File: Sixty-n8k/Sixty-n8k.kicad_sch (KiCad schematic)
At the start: 71 parts, among them J1 USB4085-GF-A_REVB, J2 SD_CARD_PORT, J3 Conn_02x32_Odd_Even, J4 Conn_01x02, SW1 RESET, SW2 DEBUG, U1 74LS05, U10 74HC164, U11 74LS393, U13 74LS148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

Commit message: Simplified design, relaid out, re-routed
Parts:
- removed C24, C25: 100nf, Capacitor_THT:C_Disc_D5.0mm_W2.5mm_P2.50mm, symbol Device:C_Small
- removed U15: 74LS138, Package_DIP:DIP-16_W7.62mm_Socket, symbol 74xx:74LS138
- removed U18: ATF16V8BQL-15PI, Package_DIP:DIP-20_W7.62mm_Socket, symbol ATF16V8BQL_15:ATF16V8BQL-15PI
- removed U5: 74LS32, Package_DIP:DIP-14_W7.62mm_Socket, symbol 74xx:74LS32
- added U12: 22V10C, Package_DIP:DIP-24_W7.62mm_Socket, symbol n8-bit-special-rescue:22V10C-6502
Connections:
- net ~{IACK} is gone; now on net ~{AS}: U16.5 (E2)
- net +5V: now also U19.9, U12.24 (VCC); no longer U16.6 (E3)
- net A16: now also U12.1 (CLK/IN1)
- net A17: now also U12.2 (IN2)
- net A18: now also U12.3 (IN3)
- net A19: now also U12.4 (IN4/PD)
- net A20: now also U12.5 (IN5)
- net A21: now also U12.6 (IN6)
- net A22: now also U12.7 (IN7)
- net A23: now also U12.8 (IN8)
- net BERR_WATCHDOG: now also RN2.2 (R1); no longer RN2.6 (R5)
- net CLK_{HALF}: now also J3.50 (Pin_50); no longer J3.18 (Pin_18)
- net D0: now also J3.6 (Pin_6); no longer J3.60 (Pin_60)
- net D1: now also J3.8 (Pin_8); no longer J3.58 (Pin_58)
- net D10: now also J3.26 (Pin_26); no longer J3.40 (Pin_40)
- net D11: now also J3.28 (Pin_28); no longer J3.38 (Pin_38)
- net D12: now also J3.30 (Pin_30); no longer J3.36 (Pin_36)
- net D13: now also J3.32 (Pin_32); no longer J3.34 (Pin_34)
- net D14: now also J3.34 (Pin_34); no longer J3.32 (Pin_32)
- net D15: now also J3.36 (Pin_36); no longer J3.30 (Pin_30)
- net D2: now also J3.10 (Pin_10); no longer J3.56 (Pin_56)
- net D3: now also J3.12 (Pin_12); no longer J3.54 (Pin_54)
- net D4: now also J3.14 (Pin_14); no longer J3.52 (Pin_52)
- net D5: now also J3.16 (Pin_16); no longer J3.50 (Pin_50)
- net D6: now also J3.18 (Pin_18); no longer J3.48 (Pin_48)
- net D7: now also J3.20 (Pin_20); no longer J3.46 (Pin_46)
- net D8: now also J3.22 (Pin_22); no longer J3.44 (Pin_44)
- net D9: now also J3.24 (Pin_24); no longer J3.42 (Pin_42)
- net FC0: now also U19.13
- net FC1: now also U19.12
- net FC2: now also U19.10
- net GND: now also U16.4 (E1), U12.12 (GND); no longer U19.10, U19.12, U19.13, U19.9
- net HALT: now also RN2.5 (R4); no longer RN2.3 (R2)
- net R~{W}: now also J3.11 (Pin_11), RN3.5 (R4), U12.15 (IO14); no longer J3.9 (Pin_9), RN3.6 (R5)
- net ~{AS}: now also J3.5 (Pin_5), RN3.2 (R1), U12.9 (IN9); no longer J3.11 (Pin_11), RN3.9 (R8), U16.4 (E1)
- net ~{BERR}: now also J3.44 (Pin_44), RN3.6 (R5); no longer J3.12 (Pin_12), RN2.5 (R4)
- net ~{BGACK}: now also J3.60 (Pin_60), RN3.8 (R7); no longer J3.28 (Pin_28), RN3.3 (R2)
- net ~{BG}: now also J3.40 (Pin_40); no longer J3.8 (Pin_8)
- net ~{BR}: now also J3.42 (Pin_42), RN3.9 (R8); no longer J3.10 (Pin_10), RN3.2 (R1)
- net ~{CS_MFP}: now also U12.23 (IO22)
- net ~{CS_XPN}: now also U12.18 (IO17)
- net ~{HALT}: now also RN2.4 (R3); no longer RN2.2 (R1)
- net ~{IACK_HI}: now also J3.58 (Pin_58); no longer J3.26 (Pin_26)
- net ~{IACK_LOW}: now also J3.56 (Pin_56); no longer J3.24 (Pin_24)
- net ~{IRQ_HI}: now also J3.54 (Pin_54), RN1.8 (R7), RN2.7 (R6); no longer J3.22 (Pin_22), RN1.3 (R2), RN3.5 (R4)
- net ~{IRQ_LOW}: now also J3.52 (Pin_52), RN1.3 (R2), RN2.3 (R2); no longer J3.20 (Pin_20), RN1.8 (R7), RN3.4 (R3)
- net ~{IRQ_MFP}: now also RN1.6 (R5); no longer RN1.5 (R4)
- net ~{LDS}: now also J3.9 (Pin_9), RN3.4 (R3), U12.10 (IN10); no longer J3.5 (Pin_5), RN3.7 (R6)
- net ~{RES}: now also RN2.6 (R5); no longer RN2.4 (R3)
- net ~{ROM_OVERLAY}: now also U12.14 (IO13)
- net ~{UDS}: now also RN3.3 (R2), U12.11 (IN11); no longer RN3.8 (R7)
- net ~{VPA}: now also RN3.7 (R6); no longer RN2.7 (R6)
- net ~{CS_RAM}_{ODD}: now reaches U4.22 (CE#), U4.24 (OE#)
- net ~{CS_RAM}_{ODD}: now also U12.19 (IO18)
- net ~{CS_RAM}_{EVEN}: now reaches U7.22 (CE#), U7.24 (OE#)
- net ~{CS_RAM}_{EVEN}: now also U12.20 (IO19)
- net ~{CS_ROM}_{EVEN}: now reaches U8.22 (~{CE}), U8.24 (~{OE})
- net ~{CS_ROM}_{EVEN}: now also U12.22 (IO21)
- net ~{CS_ROM}_{ODD}: now reaches U3.22 (~{CE}), U3.24 (~{OE})
- net ~{CS_ROM}_{ODD}: now also U12.21 (IO20)
- net IACK: now reaches U19.8
- net IACK: now also U16.6 (E3), U12.13 (IN12)
- net at U13.12 (I2): now also RN1.4 (R3); no longer RN1.7 (R6)
- net at U13.13 (I3): now also RN1.5 (R4); no longer RN1.6 (R5)
- net at U13.2 (I5): now also RN1.7 (R6); no longer RN1.4 (R3)
- net at U1.6, U13.4 (I7): now also RN1.9 (R8); no longer RN1.2 (R1)
- no-connect marks 62 -> 54
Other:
- moved on the sheet: U11C, U19A, U19B, U19C, U1G

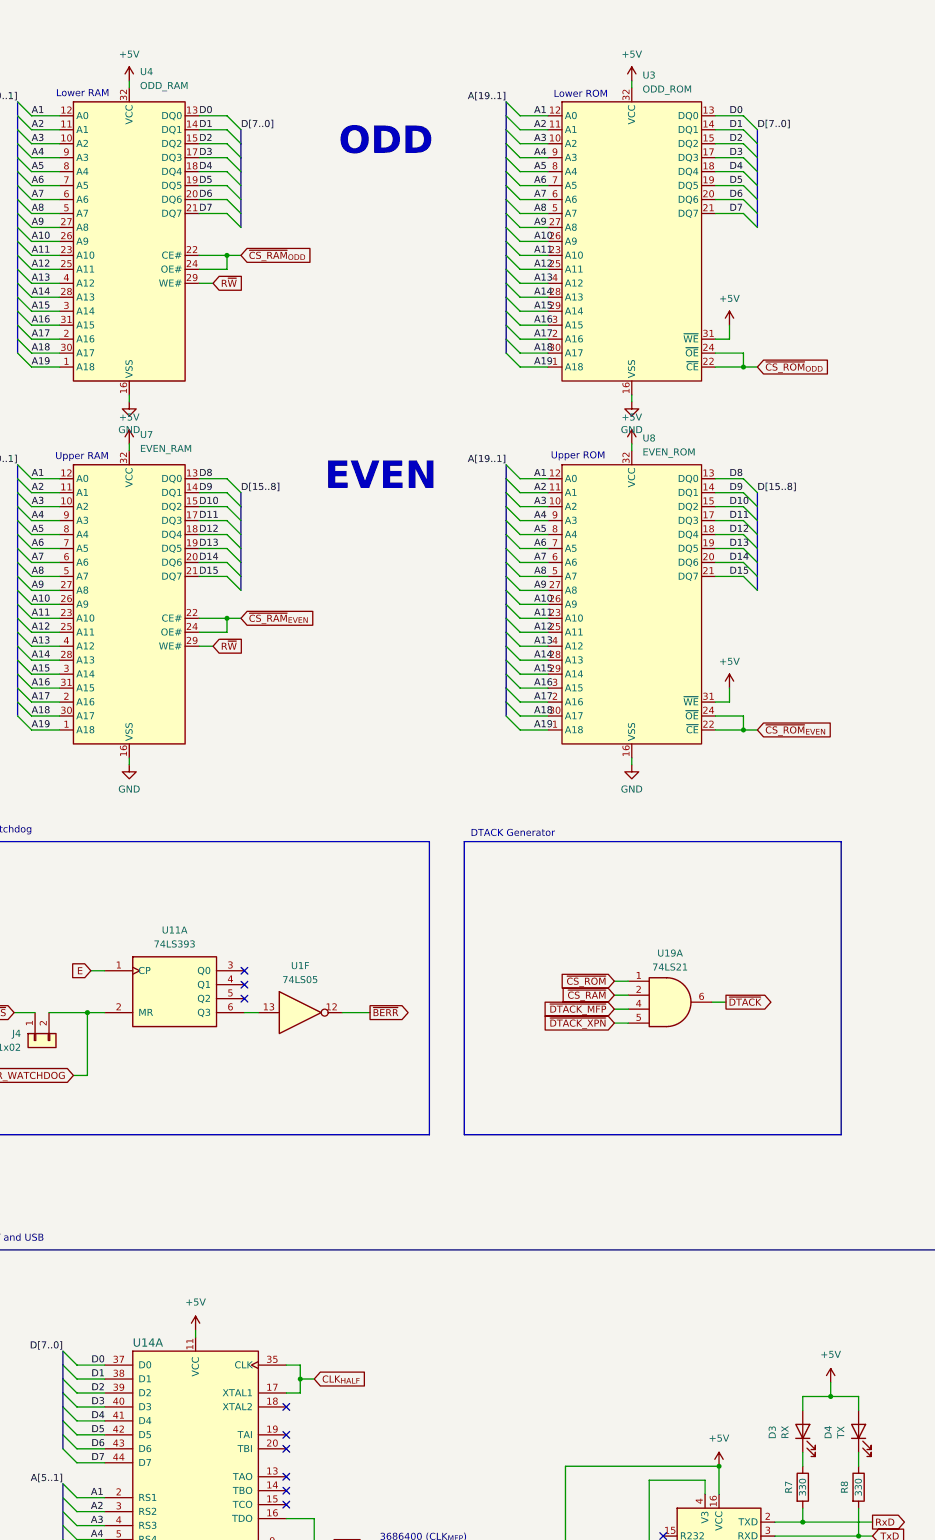
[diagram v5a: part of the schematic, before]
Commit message: More sane layout and further reductions
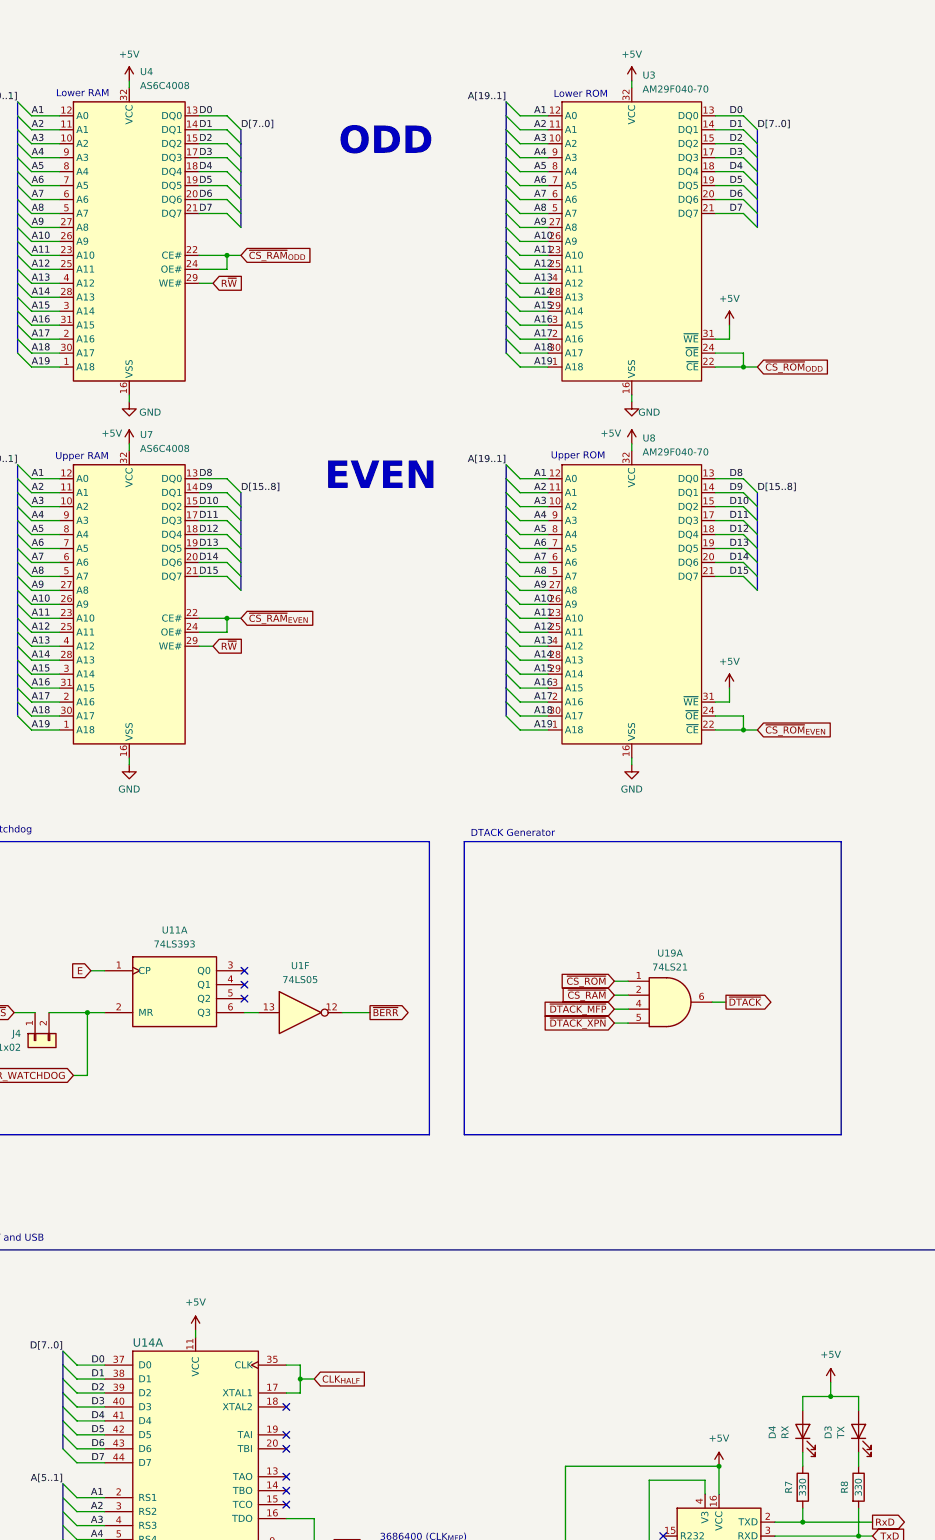
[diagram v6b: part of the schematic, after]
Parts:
- U3: value ODD_ROM -> AM29F040-70
- U4: value ODD_RAM -> AS6C4008
- U7: value EVEN_RAM -> AS6C4008
- U8: value EVEN_ROM -> AM29F040-70
- renumbered D4 to D3, D3 to D4
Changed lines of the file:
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@@
   )
   (symbol (lib_id "power:+5V") (at 431.8 95.25 0) (unit 1)
-    (in_bom yes) (on_board yes) (dnp no) (fields_autoplaced)
+    (in_bom yes) (on_board yes) (dnp no)
     (property "Reference" "#PWR020" (at 431.8 99.06 0)
       (effects (font (size 1.27 1.27)) hide)
     )
-    (property "Value" "+5V" (at 431.8 90.424 0)
+    (property "Value" "+5V" (at 427.99 93.345 0)
       (effects (font (size 1.27 1.27)))
     )
@@
       (effects (font (size 1.27 1.27)) hide)
     )
-    (property "Value" "GND" (at 340.36 92.71 0)
+    (property "Value" "GND" (at 344.17 89.535 0)
       (effects (font (size 1.27 1.27)))
     )
@@
       (effects (font (size 1.27 1.27)) (justify left))
     )
-    (property "Value" "ODD_RAM" (at 342.3159 30.099 0)
+    (property "Value" "AS6C4008" (at 342.3159 30.099 0)
       (effects (font (size 1.27 1.27)) (justify left))
     )
@@
   (symbol (lib_id "Device:LED") (at 473.075 274.955 90) (unit 1)
     (in_bom yes) (on_board yes) (dnp no)
-    (property "Reference" "D4" (at 467.5632 275.1328 0)
+    (property "Reference" "D3" (at 467.5632 275.1328 0)
       (effects (font (size 1.27 1.27)))
     )
@@
       (project "Sixty-n8k"
         (path "/899701f7-f496-45c9-a35e-7f376afd1eaf"
-          (reference "D4") (unit 1)
+          (reference "D3") (unit 1)
         )
       )
@@
   (symbol (lib_id "Device:LED") (at 462.915 274.955 90) (unit 1)
     (in_bom yes) (on_board yes) (dnp no)
-    (property "Reference" "D3" (at 457.4032 275.1328 0)
+    (property "Reference" "D4" (at 457.4032 275.1328 0)
       (effects (font (size 1.27 1.27)))
     )
@@
       (project "Sixty-n8k"
         (path "/899701f7-f496-45c9-a35e-7f376afd1eaf"
-          (reference "D3") (unit 1)
+          (reference "D4") (unit 1)
         )
       )
@@
       (effects (font (size 1.27 1.27)) (justify left))
     )
-    (property "Value" "EVEN_ROM" (at 433.7559 96.774 0)
+    (property "Value" "AM29F040-70" (at 433.7559 96.774 0)
       (effects (font (size 1.27 1.27)) (justify left))
     )
@@
   )
   (symbol (lib_id "power:GND") (at 431.8 87.63 0) (unit 1)
-    (in_bom yes) (on_board yes) (dnp no) (fields_autoplaced)
+    (in_bom yes) (on_board yes) (dnp no)
     (property "Reference" "#PWR016" (at 431.8 93.98 0)
       (effects (font (size 1.27 1.27)) hide)
     )
-    (property "Value" "GND" (at 431.8 92.71 0)
+    (property "Value" "GND" (at 434.975 89.535 0)
       (effects (font (size 1.27 1.27)))
     )
@@
       (effects (font (size 1.27 1.27)) (justify left))
     )
-    (property "Value" "ODD_ROM" (at 433.7559 30.734 0)
+    (property "Value" "AM29F040-70" (at 433.7559 30.734 0)
       (effects (font (size 1.27 1.27)) (justify left))
     )
@@
   )
   (symbol (lib_id "power:+5V") (at 340.36 95.25 0) (unit 1)
-    (in_bom yes) (on_board yes) (dnp no) (fields_autoplaced)
+    (in_bom yes) (on_board yes) (dnp no)
     (property "Reference" "#PWR019" (at 340.36 99.06 0)
       (effects (font (size 1.27 1.27)) hide)
     )
-    (property "Value" "+5V" (at 340.36 90.424 0)
+    (property "Value" "+5V" (at 337.185 93.345 0)
       (effects (font (size 1.27 1.27)))
     )
@@
       (effects (font (size 1.27 1.27)) (justify left))
     )
-    (property "Value" "EVEN_RAM" (at 342.3159 96.139 0)
+    (property "Value" "AS6C4008" (at 342.3159 96.139 0)
       (effects (font (size 1.27 1.27)) (justify left))
     )

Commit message: RC1
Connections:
- net ~{CS_RAM} is gone; now on net ~{DTACK_ROM}: U19.2
- net ~{CS_ROM} is gone; now on net ~{DTACK_RAM}: U19.1
- net ~{DTACK_ROM}: now reaches U12.16 (IO15)
- net ~{DTACK_RAM}: now reaches U12.17 (IO16)
- net ~{IACK_7}: no longer names the net of U16.7 (O7)
- no-connect marks 54 -> 53
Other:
- note removed: "TODO: Test that NMI pulse is clean"
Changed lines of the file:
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@@
   (no_connect (at 263.525 331.47))
   (no_connect (at 193.04 198.12))
-  (no_connect (at 257.81 217.17))
   (no_connect (at 368.935 283.21))
   (no_connect (at 368.935 270.51))
@@
   (no_connect (at 368.935 285.75))
   (no_connect (at 368.935 275.59))
+  (no_connect (at 263.525 336.55))
   (no_connect (at 539.115 198.755))
   (no_connect (at 368.935 311.15))
@@
   (no_connect (at 271.78 278.13))
   (no_connect (at 361.315 196.215))
-  (no_connect (at 257.81 214.63))
   (no_connect (at 437.515 294.005))
   (no_connect (at 193.04 208.28))
@@
     (stroke (width 0) (type default))
   )
+  (wire (pts (xy 257.81 217.17) (xy 260.35 217.17))
+    (stroke (width 0) (type default))
+  )
   (bus (pts (xy 223.52 194.31) (xy 223.52 196.85))
     (stroke (width 0) (type default))
@@
     (stroke (width 0) (type default))
   )
+  (wire (pts (xy 428.625 195.58) (xy 431.165 195.58))
+    (stroke (width 0) (type default))
+  )
   (wire (pts (xy 243.84 385.445) (xy 243.84 398.145))
     (stroke (width 0) (type default))
@@
     (stroke (width 0) (type default))
   )
+  (wire (pts (xy 257.81 214.63) (xy 260.35 214.63))
+    (stroke (width 0) (type default))
+  )
   (wire (pts (xy 265.43 53.34) (xy 270.51 53.34))
     (stroke (width 0) (type default))
@@
     (stroke (width 0) (type default))
   )
-  (wire (pts (xy 428.625 193.04) (xy 431.165 193.04))
-    (stroke (width 0) (type default))
-  )
   (wire (pts (xy 447.04 43.18) (xy 452.12 43.18))
     (stroke (width 0) (type default))
@@
     (stroke (width 0) (type default))
   )
-  (wire (pts (xy 428.625 195.58) (xy 431.165 195.58))
-    (stroke (width 0) (type default))
-  )
   (wire (pts (xy 265.43 96.52) (xy 270.51 96.52))
     (stroke (width 0) (type default))
@@
     (stroke (width 0) (type default))
   )
-  (wire (pts (xy 263.525 336.55) (xy 266.065 336.55))
-    (stroke (width 0) (type default))
-  )
   (wire (pts (xy 265.43 121.92) (xy 270.51 121.92))
     (stroke (width 0) (type default))
@@
     (stroke (width 0) (type default))
   )
+  (wire (pts (xy 428.625 193.04) (xy 431.165 193.04))
+    (stroke (width 0) (type default))
+  )
   (wire (pts (xy 238.76 260.35) (xy 238.76 280.67))
     (stroke (width 0) (type default))
@@
     (effects (font (size 1.27 1.27)) (justify left bottom))
   )
-  (text "TODO: Test that NMI pulse is clean" (at 164.465 273.05 0)
-    (effects (font (size 1.27 1.27)) (justify left bottom))
-  )
   (text "Address Decoding" (at 155.575 166.37 0)
     (effects (font (size 1.27 1.27)) (justify left bottom))
@@
     )
   )
+  (global_label "~{DTACK_RAM}" (shape output) (at 260.35 214.63 0) (fields_autoplaced)
+    (effects (font (size 1.27 1.27)) (justify left))
+    (property "Intersheetrefs" "${INTERSHEET_REFS}" (at 273.8996 214.63 0)
+      (effects (font (size 1.27 1.27)) (justify left) hide)
+    )
+  )
   (global_label "CLK_{CPU}" (shape input) (at 212.09 35.56 180) (fields_autoplaced)
     (effects (font (size 1.27 1.27)) (justify right))
@@
     )
   )
+  (global_label "~{DTACK_RAM}" (shape input) (at 428.625 193.04 180) (fields_autoplaced)
+    (effects (font (size 1.27 1.27)) (justify right))
+    (property "Intersheetrefs" "${INTERSHEET_REFS}" (at 415.0754 193.04 0)
+      (effects (font (size 1.27 1.27)) (justify right) hide)
+    )
+  )
   (global_label "~{IRQ_MFP}" (shape input) (at 224.155 275.59 180) (fields_autoplaced)
     (effects (font (size 1.27 1.27)) (justify right))
@@
     )
   )
+  (global_label "~{DTACK_ROM}" (shape output) (at 260.35 217.17 0) (fields_autoplaced)
+    (effects (font (size 1.27 1.27)) (justify left))
+    (property "Intersheetrefs" "${INTERSHEET_REFS}" (at 274.1415 217.17 0)
+      (effects (font (size 1.27 1.27)) (justify left) hide)
+    )
+  )
   (global_label "R~{W}" (shape input) (at 333.375 311.15 180) (fields_autoplaced)
     (effects (font (size 1.27 1.27)) (justify right))
@@
     )
   )
-  (global_label "~{CS_ROM}" (shape input) (at 428.625 193.04 180) (fields_autoplaced)
-    (effects (font (size 1.27 1.27)) (justify right))
-    (property "Intersheetrefs" "${INTERSHEET_REFS}" (at 418.2202 193.04 0)
-      (effects (font (size 1.27 1.27)) (justify right) hide)
-    )
-  )
   (global_label "IACK" (shape input) (at 260.35 224.79 0) (fields_autoplaced)
     (effects (font (size 1.27 1.27)) (justify left))
@@
     )
   )
+  (global_label "~{DTACK_ROM}" (shape input) (at 428.625 195.58 180) (fields_autoplaced)
+    (effects (font (size 1.27 1.27)) (justify right))
+    (property "Intersheetrefs" "${INTERSHEET_REFS}" (at 414.8335 195.58 0)
+      (effects (font (size 1.27 1.27)) (justify right) hide)
+    )
+  )
   (global_label "CLK_{CPU}" (shape output) (at 63.5 203.2 0) (fields_autoplaced)
     (effects (font (size 1.27 1.27)) (justify left))
@@
     )
   )
-  (global_label "~{IACK_7}" (shape output) (at 266.065 336.55 0) (fields_autoplaced)
-    (effects (font (size 1.27 1.27)) (justify left))
-    (property "Intersheetrefs" "${INTERSHEET_REFS}" (at 275.3813 336.55 0)
-      (effects (font (size 1.27 1.27)) (justify left) hide)
-    )
-  )
   (global_label "~{RES}" (shape input) (at 167.64 198.12 180) (fields_autoplaced)
     (effects (font (size 1.27 1.27)) (justify right))
@@
       (effects (font (size 1.27 1.27)) (justify right) hide)
     )
-  )
-  (global_label "~{CS_RAM}" (shape input) (at 428.625 195.58 180) (fields_autoplaced)
-    (effects (font (size 1.27 1.27)) (justify right))
-    (property "Intersheetrefs" "${INTERSHEET_REFS}" (at 418.4621 195.58 0)
-      (effects (font (size 1.27 1.27)) (justify right) hide)
-    )

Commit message: Adds GAL logic
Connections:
- net ~{LDS}: now also U12.11 (IN11); no longer U12.10 (IN10)
- net ~{UDS}: now also U12.10 (IN10); no longer U12.11 (IN11)
- net ~{DTACK_RAM} renamed ~{CS_RAM}
- net ~{DTACK_ROM} renamed ~{CS_ROM}
- no-connect marks 53 -> 54
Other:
- note added: "Default Memory Map: MFP: $E00000...$EFFFFF XPN: $800000...$8FFFFF ROM: $400000...$4FFFFF (overlaid on RAM during bootup!) RAM: $000000...$0FFFFF"
- note removed: "Default Memory Map: MFP: $E00000...$E10000 ROM: $400000...$4FFFFF (overlaid on RAM during bootup!) RAM: $000000...$0FFFFF"
- moved on the sheet: C1, C10, C11, C12, C13, C14, C15, C16, C17, C18, C19, C2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
